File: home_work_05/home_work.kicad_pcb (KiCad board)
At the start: 2 copper layers, 45 x 30 mm, 7 parts, among them J1 Conn_01x02_Pin, J2 Screw_Terminal_01x02, Q1 BC337-40

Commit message: update pcb
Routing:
- net GND: track 16.5 -> 0.66 mm
- added copper zone on F.Cu, net GND
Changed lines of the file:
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@@
-	)
-	(segment
-		(start 150.445 59.945)
-		(end 140.5 59.945)
-		(width 0.5)
-		(layer "F.Cu")
-		(net 4)
 	)
 	(segment
@@
 		(start 150.5 60)
 		(end 150.445 59.945)
-		(width 0.5)
-		(layer "F.Cu")
-		(net 4)
-	)
-	(segment
-		(start 140.5 54)
-		(end 140.5 59.945)
 		(width 0.5)
 		(layer "F.Cu")
@@
 		(net 5)
 	)
+	(zone
+		(net 4)
+		(net_name "GND")
+		(layer "F.Cu")
+		(hatch edge 0.5)
+		(connect_pads
+			(clearance 0.5)
+		)
+		(min_thickness 0.25)
+		(filled_areas_thickness no)
+		(fill yes
+			(thermal_gap 0.5)
+			(thermal_bridge_width 0.5)
+		)
+		(polygon
+			(pts
+				(xy 111.5 48) (xy 155.5 48) (xy 155.5 77) (xy 111.5 77)
+			)
+		)
+	)
 )

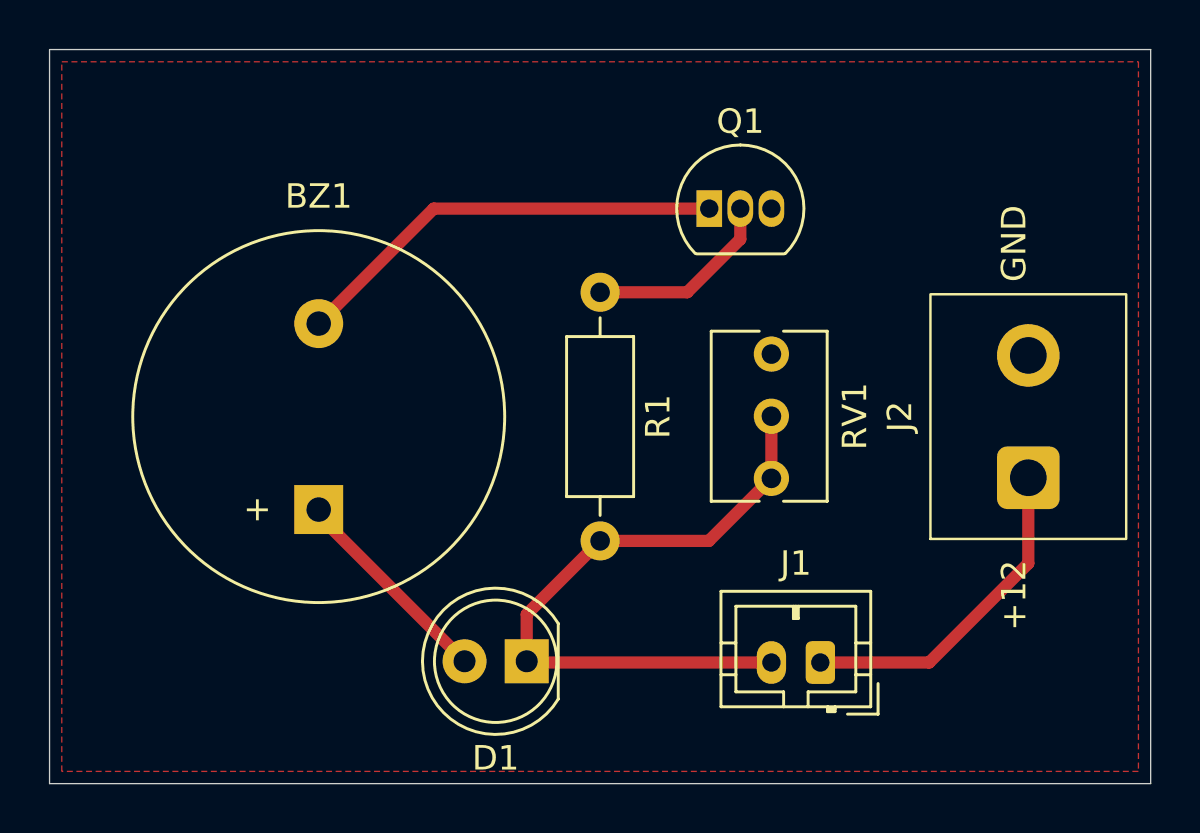
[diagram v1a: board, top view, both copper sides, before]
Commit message: update pcb and footprint
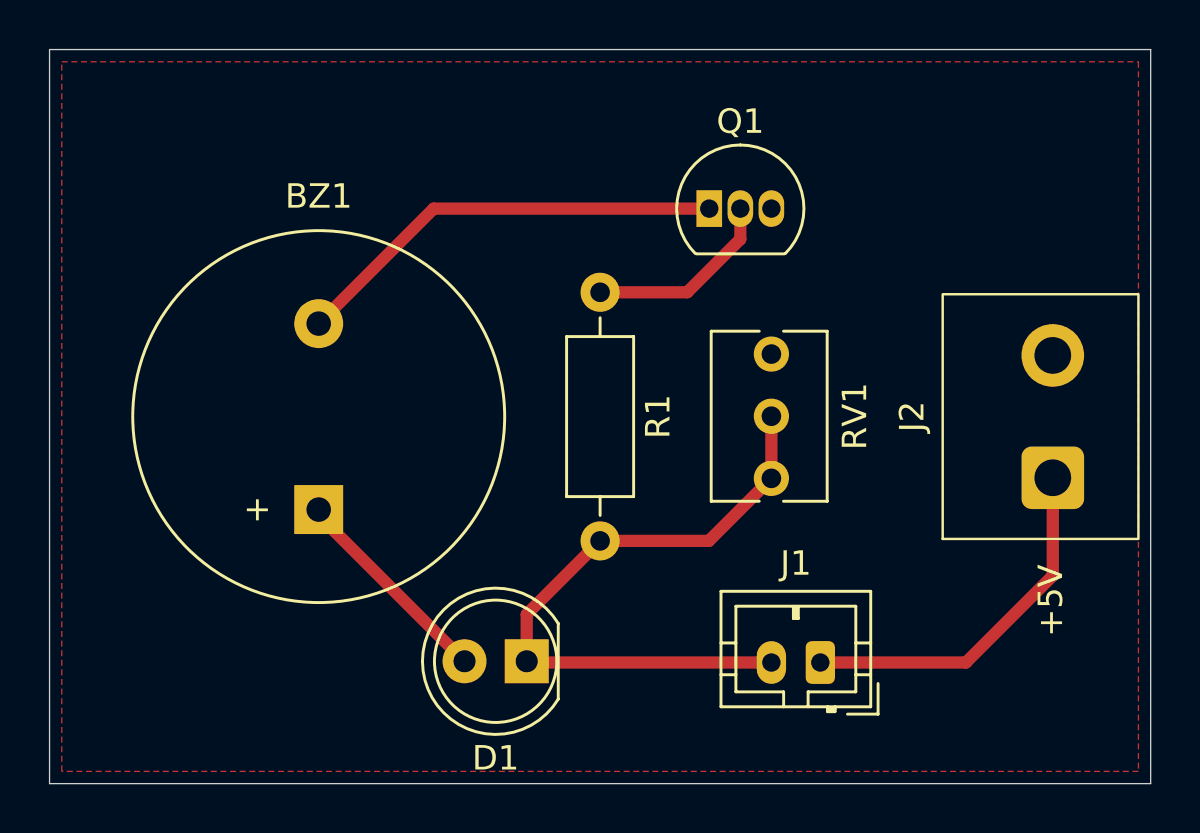
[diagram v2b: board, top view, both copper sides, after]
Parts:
- moved J2 1.00 mm to (152.0, 62.5)
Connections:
- net +12V renamed +5V
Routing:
- net +5V: track 22.3 -> 23.6 mm
- net GND: track 0.66 -> 0.08 mm
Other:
- board text added: "+5V"
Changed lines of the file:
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@@
 	)
 	(net 0 "")
-	(net 1 "+12V")
+	(net 1 "+5V")
 	(net 2 "Net-(BZ1--)")
 	(net 3 "Net-(D1-K)")
@@
 			(remove_unused_layers no)
 			(roundrect_rratio 0.208333)
-			(net 1 "+12V")
+			(net 1 "+5V")
 			(pinfunction "Pin_1")
 			(pintype "passive")
@@
 			(layers "*.Cu" "*.Mask")
 			(remove_unused_layers no)
-			(net 1 "+12V")
+			(net 1 "+5V")
 			(pinfunction "+")
 			(pintype "passive")
@@
 			(layers "*.Cu" "*.Mask")
 			(remove_unused_layers no)
-			(net 1 "+12V")
+			(net 1 "+5V")
 			(pinfunction "A")
 			(pintype "passive")
@@
 	(footprint "mipt:FK301-5.0"
 		(layer "F.Cu")
-		(at 151 62.5 90)
+		(at 152 62.5 90)
 		(property "Reference" "J2"
-			(at 0 -5.25 90)
+			(at 0 -5.75 90)
 			(unlocked yes)
 			(layer "F.SilkS")
@@
 		(attr through_hole)
 		(fp_rect
-			(start -5 -4)
-			(end 5 4)
+			(start -5 -4.5)
+			(end 5 3.5)
 			(stroke
 				(width 0.1)
@@
 		)
 		(fp_rect
-			(start -5.25 -4.25)
-			(end 5.25 4.25)
+			(start -5.25 -4.75)
+			(end 5.25 3.75)
 			(stroke
 				(width 0.05)
@@
 			(fill none)
 			(layer "F.CrtYd")
-		)
-		(fp_text user "GND"
-			(at 5.5 0 90)
-			(unlocked yes)
-			(layer "F.SilkS")
-			(effects
-				(font
-					(size 1 1)
-					(thickness 0.1)
-				)
-				(justify left bottom)
-			)
-		)
-		(fp_text user "+12"
-			(at -8.75 0 90)
-			(unlocked yes)
-			(layer "F.SilkS")
-			(effects
-				(font
-					(size 1 1)
-					(thickness 0.1)
-				)
-				(justify left bottom)
-			)
 		)
 		(fp_text user "${REFERENCE}"
@@
 			(remove_unused_layers no)
 			(roundrect_rratio 0.1640419948)
-			(net 1 "+12V")
+			(net 1 "+5V")
 			(pinfunction "Pin_1")
 			(pintype "passive")
@@
 		(stroke
 			(width 0.05)
-			(type default)
+			(type solid)
 		)
 		(fill none)
 		(layer "Edge.Cuts")
 	)
+	(gr_text "+5V"
+		(at 152.5 71.5 90)
+		(layer "F.SilkS")
+		(effects
+			(font
+				(size 1 1)
+				(thickness 0.1)
+			)
+			(justify left bottom)
+		)
+	)
 	(segment
-		(start 151 68.5)
-		(end 151 65)
+		(start 148.45 72.55)
+		(end 152 69)
+		(width 0.5)
+		(layer "F.Cu")
+		(net 1)
+	)
+	(segment
+		(start 142.5 72.55)
+		(end 148.45 72.55)
 		(width 0.5)
 		(layer "F.Cu")
@@
 	)
 	(segment
-		(start 146.95 72.55)
-		(end 151 68.5)
+		(start 152 69)
+		(end 152 65)
 		(width 0.5)
 		(layer "F.Cu")
@@
 	)
 	(segment
-		(start 142.5 72.55)
-		(end 146.95 72.55)
-		(width 0.5)
-		(layer "F.Cu")
-		(net 1)
-	)
-	(segment
 		(start 126.7 54)
 		(end 137.96 54)
@@
 	)
 	(segment
-		(start 151 60)
-		(end 150.5 60)
-		(width 0.5)
-		(layer "F.Cu")
-		(net 4)
-	)
-	(segment
 		(start 140.555 60)
 		(end 140.5 59.945)
@@
 		(layer "F.Cu")
 		(net 4)
-	)
-	(segment
-		(start 150.5 60)
-		(end 150.445 59.945)
-		(width 0.5)
-		(layer "F.Cu")
-		(net 4)

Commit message: update home work 05
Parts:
- R1: value R -> 33K
- RV1: value R_Potentiometer -> 1M
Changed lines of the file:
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@@
 			)
 		)
-		(property "Value" "R"
+		(property "Value" "33K"
 			(at 5.08 2.37 90)
-			(layer "F.Fab")
+			(layer "F.SilkS")
 			(effects
 				(font
@@
 			)
 		)
-		(property "Value" "R_Potentiometer"
+		(property "Value" "1M"
 			(at -2.54 3.59 90)
 			(layer "F.Fab")
@@
 		)
 		(property "Value" "Buzzer"
-			(at -4.7 0 180)
-			(layer "F.Fab")
+			(at -5.2 0 180)
+			(layer "F.SilkS")
 			(effects
 				(font
@@
 		)
 		(property "Value" "BC337-40"
-			(at 1.27 2.79 0)
-			(layer "F.Fab")
-			(effects
+			(at 1.04 2.5 0)
+			(layer "F.Fab")
+			(effects
